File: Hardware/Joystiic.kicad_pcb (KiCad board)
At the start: 2 copper layers, 25.4 x 50.8 mm, 21 parts, among them J1 Qwiic_Connector, J2 Qwiic_Connector, J3 I2C_Standard_PTH_Connector, J4 AVR_SPI_PROG_3X2TESTPOINTS, U1 ATTINY85-20SU, U2 SPARKX-LOGO4, U3 SPARKX-LOGO4, U4 CC_LICENSE

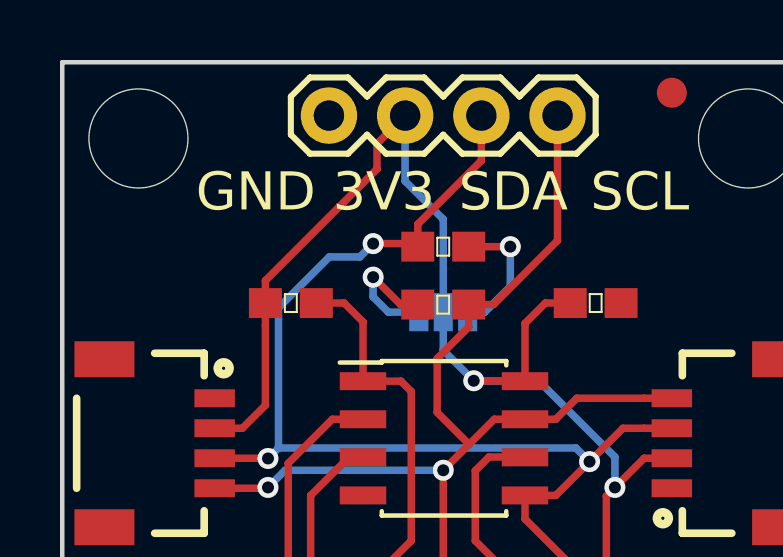
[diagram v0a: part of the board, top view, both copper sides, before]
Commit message: Panelized
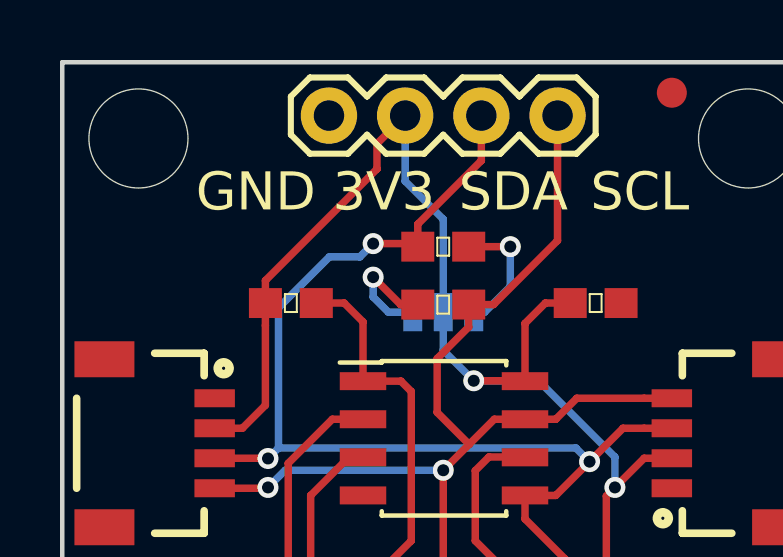
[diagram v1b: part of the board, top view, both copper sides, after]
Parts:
- JP1: footprint Jumpers:SMT-JUMPER_3_2-NC_PASTE_SILK -> Jumpers:SMT-JUMPER_3_2-NC_TRACE_SILK
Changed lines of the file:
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@@
     (links 35)
     (no_connects 0)
-    (area 61.246229 67.4287 173.174 145.2582)
+    (area 133.476572 83.4942 194.1544 149.7794)
     (thickness 1.6)
     (drawings 31)
@@
       (net 1 GND) (solder_mask_margin 0.1016))
   )
-  (module Jumpers:SMT-JUMPER_3_2-NC_PASTE_SILK (layer B.Cu)
-    (at 149.86 99.7712)
-    (attr smd)
-    (fp_text reference JP1 (at 0 1.651) (layer B.Fab)
-      (effects (font (size 0.6096 0.6096) (thickness 0.127)) (justify mirror))
-    )
-    (fp_text value JUMPER-SMT_3_2-NC_PASTE_SILK (at -0.2032 -1.6764) (layer F.Fab)
-      (effects (font (size 0.6096 0.6096) (thickness 0.127)))
-    )
-    (fp_line (start -1.397 0.889) (end -1.397 -0.889) (layer B.Paste) (width 0.508))
-    (fp_line (start 1.397 -0.889) (end 1.397 0.889) (layer B.Paste) (width 0.508))
-    (fp_line (start -1.397 -0.889) (end 1.397 -0.889) (layer B.Paste) (width 0.508))
-    (fp_line (start -1.397 -0.635) (end 1.397 -0.635) (layer B.Paste) (width 0.508))
-    (fp_line (start -1.397 -0.127) (end 1.397 -0.127) (layer B.Paste) (width 0.508))
-    (fp_line (start -1.397 0.381) (end 1.397 0.381) (layer B.Paste) (width 0.508))
-    (fp_line (start -1.397 0.889) (end 1.397 0.889) (layer B.Paste) (width 0.508))
-    (fp_line (start 1.27 -1.016) (end -1.27 -1.016) (layer B.SilkS) (width 0.1524))
-    (fp_line (start 1.524 -0.762) (end 1.524 0.762) (layer B.SilkS) (width 0.1524))
-    (fp_line (start -1.524 -0.762) (end -1.524 0.762) (layer B.SilkS) (width 0.1524))
-    (fp_line (start -1.27 1.016) (end 1.27 1.016) (layer B.SilkS) (width 0.1524))
-    (fp_arc (start 1.27 0.762) (end 1.27 1.016) (angle -90) (layer B.SilkS) (width 0.1524))
-    (fp_arc (start -1.27 0.762) (end -1.524 0.762) (angle -90) (layer B.SilkS) (width 0.1524))
-    (fp_arc (start -1.27 -0.762) (end -1.27 -1.016) (angle -90) (layer B.SilkS) (width 0.1524))
-    (fp_arc (start 1.27 -0.762) (end 1.524 -0.762) (angle -90) (layer B.SilkS) (width 0.1524))
-    (pad 1 smd rect (at -0.8128 0) (size 0.635 1.27) (layers B.Cu B.Mask)
-      (net 2 "Net-(JP1-Pad1)") (solder_mask_margin 0.1016))
-    (pad 2 smd rect (at 0 0) (size 0.635 1.27) (layers B.Cu B.Mask)
-      (net 4 3.3V) (solder_mask_margin 0.1016))
-    (pad 3 smd rect (at 0.8128 0) (size 0.635 1.27) (layers B.Cu B.Mask)
-      (net 3 "Net-(JP1-Pad3)") (solder_mask_margin 0.1016))
-  )
   (module Resistors:0603 (layer F.Cu)
     (at 144.78 99.4664)
@@
     )
   )
+  (module Jumpers:SMT-JUMPER_3_2-NC_TRACE_SILK (layer B.Cu)
+    (at 149.86 99.7712)
+    (attr smd)
+    (fp_text reference JP1 (at 0 1.524) (layer F.Fab)
+      (effects (font (size 0.6096 0.6096) (thickness 0.127)))
+    )
+    (fp_text value JUMPER-SMT_3_2-NC_PASTE_SILK (at 0 -1.651) (layer F.Fab)
+      (effects (font (size 0.6096 0.6096) (thickness 0.127)))
+    )
+    (fp_line (start 1.27 -1.016) (end -1.27 -1.016) (layer B.SilkS) (width 0.1524))
+    (fp_line (start 1.7272 -0.5588) (end 1.7272 0.5588) (layer B.SilkS) (width 0.1524))
+    (fp_line (start -1.7272 -0.5588) (end -1.7272 0.5588) (layer B.SilkS) (width 0.1524))
+    (fp_line (start -1.27 1.016) (end 1.27 1.016) (layer B.SilkS) (width 0.1524))
+    (fp_line (start 0 0) (end 1.016 0) (layer B.Cu) (width 0.254))
+    (fp_line (start 0 0) (end -1.016 0) (layer B.Cu) (width 0.254))
+    (fp_arc (start 1.27 0.5588) (end 1.27 1.016) (angle -90) (layer B.SilkS) (width 0.1524))
+    (fp_arc (start -1.27 0.5588) (end -1.7272 0.5588) (angle -90) (layer B.SilkS) (width 0.1524))
+    (fp_arc (start -1.27 -0.5588) (end -1.27 -1.016) (angle -90) (layer B.SilkS) (width 0.1524))
+    (fp_arc (start 1.27 -0.5588) (end 1.7272 -0.5588) (angle -90) (layer B.SilkS) (width 0.1524))
+    (pad 1 smd rect (at -1.016 0) (size 0.635 1.27) (layers B.Cu B.Mask)
+      (net 2 "Net-(JP1-Pad1)") (solder_mask_margin 0.1016))
+    (pad 2 smd rect (at 0 0) (size 0.635 1.27) (layers B.Cu B.Mask)
+      (net 4 3.3V) (solder_mask_margin 0.1016))
+    (pad 3 smd rect (at 1.016 0) (size 0.635 1.27) (layers B.Cu B.Mask)
+      (net 3 "Net-(JP1-Pad3)") (solder_mask_margin 0.1016))
+  )
   (gr_text _ (at 152.4 107.3404) (layer B.SilkS)
     (effects (font (size 1.27 1.27) (thickness 0.254)) (justify mirror))
@@
     (effects (font (size 1.27 1.27) (thickness 0.254)) (justify mirror))
   )
-  (gr_text SCL (at 156.4132 95.758) (layer B.SilkS)
+  (gr_text SCL (at 153.7208 96.4184 90) (layer B.SilkS)
     (effects (font (size 1.27 1.27) (thickness 0.254)) (justify mirror))
   )
-  (gr_text "SDA\n" (at 152.1968 95.758) (layer B.SilkS)
+  (gr_text "SDA\n" (at 151.2316 96.4692 90) (layer B.SilkS)
     (effects (font (size 1.27 1.27) (thickness 0.254)) (justify mirror))
   )
-  (gr_text "3V3\n" (at 147.8788 95.758) (layer B.SilkS)
+  (gr_text "3V3\n" (at 148.7424 96.4692 90) (layer B.SilkS)
     (effects (font (size 1.27 1.27) (thickness 0.254)) (justify mirror))
   )
-  (gr_text "GND\n" (at 143.6116 95.758 360) (layer B.SilkS)
+  (gr_text "GND\n" (at 146.1008 96.5708 90) (layer B.SilkS)
     (effects (font (size 1.27 1.27) (thickness 0.254)) (justify mirror))
   )
@@
     (effects (font (size 1.27 1.27) (thickness 0.254)))
   )
-  (gr_text "GND\n" (at 143.6116 95.758 360) (layer F.SilkS)
+  (gr_text "GND\n" (at 143.6116 95.758) (layer F.SilkS)
     (effects (font (size 1.27 1.27) (thickness 0.254)))
   )

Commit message: v1.1
- Buzzard Silkscreen
- Wide SOIC footprint
- Power LED
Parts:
- added ?: , buzzard_labels (30):GND3, F.Cu at (141.7, 95.6)
- added ?: , buzzard_labels (29):SCL3, B.Cu at (153.7, 98.0)
- added ?: , buzzard_labels (29):I#C_PU4, B.Cu at (152.9, 102.0)
- added ?: , buzzard_labels (29):QWIIC5, B.Cu at (152.7, 127.8)
- added ?: , buzzard_labels (29):JOYSTIIC6, B.Cu at (153.4, 129.7)
- added ?: , buzzard_labels (32):PWR0, F.Cu at (161.3, 121.9)
- added ?: , buzzard_labels (30):3V30, F.Cu at (145.8, 95.6)
- added ?: , buzzard_labels (30):SDA1, F.Cu at (149.5, 95.6)
- added ?: , buzzard_labels (30):SCL2, F.Cu at (153.4, 95.6)
- added ?: , buzzard_labels (31):HORZ1, F.Cu at (144.1, 114.1)
- added ?: , buzzard_labels (31):VERT0, F.Cu at (142.8, 121.0)
- added ?: , buzzard_labels (29):GND0, B.Cu at (146.1, 98.4)
- added ?: , buzzard_labels (29):3V31, B.Cu at (148.6, 98.0)
- added ?: , buzzard_labels (29):SDA2, B.Cu at (151.1, 98.2)
- added D1: LED-RED0603, LEDs:LED_0603, F.Cu at (159.3, 119.3)
- added R4: 470OHM-0603-1_10W-1%, Resistors:0603, F.Cu at (157.3, 119.2)
- U1: footprint Housings_SOIC:SOIC-8_3.9x4.9mm_Pitch1.27mm -> attiny85 (1):ATTINY85
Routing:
- net 3.3V: track 84.3 -> 97.9 mm
- net /HORIZONTAL: track 37.9 -> 40.9 mm
- net Net-(D1-PadA): track 0.00 -> 1.83 mm
- net /RESET: track 12.6 -> 13.8 mm
- net /SDA: track 42.6 -> 43.8 mm
- net /SELECT: track 17.3 -> 18.4 mm
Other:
- board text removed: "3V3"
- board text removed: "GND"
- board text removed: "H"
- board text removed: "I2C PU"
- board text removed: "Qwiic Joystiic"
- board text removed: "SCL"
- board text removed: "SDA"
- board text removed: "V"
